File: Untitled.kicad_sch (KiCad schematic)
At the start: 1 part, among them U1 ICE40LP8K-CM121

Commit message: Move tinyfpga components to main schem
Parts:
- added C1, C10, C15, C6: 1uF, Capacitors_SMD:C_0402_NoSilk, symbol TinyFPGA-BX-rescue:C
- added C11, C16, C17: 100nF, Capacitors_SMD:C_0402_NoSilk, symbol TinyFPGA-BX-rescue:C
- added C12, C13, C7, C9: 10nF, Capacitors_SMD:C_0402_NoSilk, symbol TinyFPGA-BX-rescue:C_Small
- added C14, C2, C3, C4: 100nF, Capacitors_SMD:C_0402_NoSilk, symbol TinyFPGA-BX-rescue:C_Small
- added C5, C8: 10uF, Capacitors_SMD:C_0603, symbol TinyFPGA-BX-rescue:C
- added D1, D2: LED_Small, LEDs:LED_0603, symbol TinyFPGA-BX-rescue:LED_Small
- added J1: USB_OTG, Connectors:USB_Micro-B, symbol TinyFPGA-BX-rescue:USB_OTG
- added J2: Conn_02x03_Odd_Even, Pin_Headers:Pin_Header_Straight_2x03_Pitch2.54mm_SMD, symbol TinyFPGA-BX-rescue:Conn_02x03_Odd_Even
- added J3: Conn_02x08_Odd_Even, Pin_Headers:Pin_Header_Straight_2x08_Pitch2.54mm_SMD, symbol TinyFPGA-BX-rescue:Conn_02x08_Odd_Even
- added J4, J5: CONN_01X14, Pin_Headers:Pin_Header_Straight_1x14_Pitch2.54mm, symbol TinyFPGA-BX-rescue:Conn_01x14
- added L1: Bead, Inductors_SMD:L_0603, symbol TinyFPGA-BX-rescue:Ferrite_Bead_Small
- added R1: 100, Resistors_SMD:R_0402_NoSilk, symbol TinyFPGA-BX-rescue:R
- added R10, R7, R8: 10k, Resistors_SMD:R_0402_NoSilk, symbol TinyFPGA-BX-rescue:R
- added R2: 1.5k, Resistors_SMD:R_0402_NoSilk, symbol TinyFPGA-BX-rescue:R
- added R3, R4: 68, Resistors_SMD:R_0402_NoSilk, symbol TinyFPGA-BX-rescue:R
- added R5, R6: 270, Resistors_SMD:R_0402_NoSilk, symbol TinyFPGA-BX-rescue:R_Small
- added R9: R, Resistors_SMD:R_0402, symbol TinyFPGA-BX-rescue:R
- added SW1: SW_Push, tinyfpga:PTS_810_SMT_Switch, symbol TinyFPGA-BX-rescue:SW_Push
- added TP1, TP2, TP3: TEST, Measurement_Points:Measurement_Point_Round-SMD-Pad_Small, symbol TinyFPGA-BX-rescue:TEST
- added U2: MIC5504-3.3YM5-TR, tinyfpga:SC-70-C5, symbol TinyFPGA-BX-rescue:MIC5504-3.3YM5-TR
- added U3: MIC5365-1.2YC5-TR, tinyfpga:SC-70-C5, symbol TinyFPGA-BX-rescue:MIC5365-1.2YC5-TR
- added U4: iCE40-LP8K-CM81, tinyfpga:CM81, symbol TinyFPGA-BX-rescue:iCE40-LP8K-CM81
- added U5: DSC6001CI2A-016.0000T, tinyfpga:CDFN3225-4LD-PL-1, symbol TinyFPGA-BX-rescue:DSC6001CI2A-016.0000T
- added U6: AT25SF081-SSHD-B, Housings_SOIC:SOIC-8-1EP_3.9x4.9mm_Pitch1.27mm, symbol TinyFPGA-BX-rescue:AT25SF041-SSHD-B
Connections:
- new net: J1.2 (D-), R4.2
- new net: D1.1 (K), R5.1
- new net: C11.1, C8.1, U4.J6 (GNDPLL0)
- new net: C11.2, C8.2, R1.1, U4.J7 (VCCPLL0)
- new net: D2.1 (K), R6.1
- new net: J1.1 (VBUS), L1.2
- new net: J1.3 (D+), R2.1, R3.2
- new net +1V2: C15.1, C4.1, C7.1, C9.1, R1.2, TP1.1, U3.5 (VOUT), U4.D4 (VCC), U4.E3 (IOL_14A_GBIN6), U4.E9 (VCC), U4.F1 (IOL_22A), U4.F2 (VCC)
- new net +3V3: C10.1, C12.1, C13.1, C14.1, C16.1, C17.1, C2.1, C3.1, C6.1, D1.2 (A), J3.3 (Pin_3), J5.3 (Pin_3), R10.1, R7.1, R8.1, R9.1, U2.4 (NC), U2.5 (VOUT), U3.1 (VIN), U3.3 (EN), U4.A5 (VCCIO_0), U4.B5 (IOT_188), U4.B9 (IOR_120), U4.C6 (VCCIO_1), U4.C8 (VPP_2V5), U4.H3 (VCCIO_3), U4.H8 (VCC_SPI), U4.J5 (VCCIO_2), U5.1 (OE), U5.4 (VDD), U6.8 (VCC)
- new net +5V: C1.1, C5.1, J5.1 (Pin_1), L1.1, U2.1 (VIN), U2.3 (EN)
- new net 109: J3.9 (Pin_9), R8.2, U4.J8 (IOR_109), U6.7 (!HOLD)
- new net 10A: J4.8 (Pin_8), U4.D1 (IOL_10A)
- new net 10B: J4.10 (Pin_10), U4.E1 (IOL_10B)
- new net 110: J3.5 (Pin_5), U4.J9 (IOR_110)
- new net 111: J5.14 (Pin_14), U4.H9 (IOR_111)
- new net 112: J3.7 (Pin_7), U4.G9 (IOR_112)
- new net 115: U4.D6 (IOR_115)
- new net 116: J5.10 (Pin_10), U4.A9 (IOR_116)
- new net 119: J5.13 (Pin_13), U4.D9 (IOR_119)
- new net 13A: J4.9 (Pin_9), U4.E2 (IOL_13A)
- new net 140: J3.1 (Pin_1), U4.E8 (IOR_140_GBIN3)
- new net 141: J5.12 (Pin_12), U4.D8 (IOR_141_GBIN2)
- new net 148: J5.11 (Pin_11), U4.C9 (IOR_148)
- new net 170: J5.9 (Pin_9), U4.B8 (IOT_170)
- new net 174: J5.8 (Pin_8), U4.A8 (IOT_174)
- new net 177: J5.6 (Pin_6), U4.A7 (IOT_177)
- new net 180: J5.7 (Pin_7), U4.B7 (IOT_180)
- new net 183: J5.5 (Pin_5), U4.B6 (IOT_183)
- new net 185: J5.4 (Pin_4), U4.A6 (IOT_185)
- new net 212: U4.D5 (IOT_212)
- new net 221: J4.2 (Pin_2), U4.A2 (IOT_221)
- new net 224: J4.3 (Pin_3), U4.A1 (IOT_224)
- new net 24A: U4.G3 (IOL_24A)
- new net 24B: J3.2 (Pin_2), U4.G1 (IOL_24B)
- new net 26A: J4.11 (Pin_11), U4.G2 (IOL_26A)
- new net 26B: J4.14 (Pin_14), U4.H2 (IOL_26B)
- new net 2A: J4.5 (Pin_5), U4.C2 (IOL_2A)
- new net 3A: J4.4 (Pin_4), U4.B1 (IOL_3A)
- new net 3B: J4.6 (Pin_6), U4.C1 (IOL_3B)
- new net 54: J4.12 (Pin_12), U4.H1 (IOB_54)
- new net 55: J4.13 (Pin_13), U4.J1 (IOB_55)
- new net 56: J2.2 (Pin_2), U4.J2 (IOB_56)
- new net 57: J3.6 (Pin_6), U4.J3 (IOB_57)
- new net 70: J3.8 (Pin_8), U4.J4 (IOB_70)
- new net 7A: J4.7 (Pin_7), U4.D2 (IOL_7A)
- new net 81_GBIN5: U4.G4 (IOB_81_GBIN5)
- new net 82: J3.10 (Pin_10), R7.2, TP2.1, U4.H4 (IOB_82_GBIN4), U6.3 (!WP)
- new net CDONE: U4.E6 (CDONE)
- new net CLK: J2.1 (Pin_1), U4.B2 (IOL_2B), U5.3 (OUT)
- new net CRESET_B: R9.2, SW1.2, TP3.1, U4.H6 (CRESET_B)
- new net GND: C1.2, C10.2, C12.2, C13.2, C14.2, C15.2, C16.2, C17.2, C2.2, C3.2, C4.2, C5.2, C6.2, C7.2, C9.2, J1.5 (GND), J1.6 (Shield), J3.15 (Pin_15), J3.16 (Pin_16), J3.4 (Pin_4), J4.1 (Pin_1), J5.2 (Pin_2), R5.2, R6.2, SW1.1, U2.2 (GND), U3.2 (GND), U4.E4 (IOL_14B), U4.E5 (IOT_214), U4.F4 (GND), U4.F5 (GND), U4.F6 (GND), U4.F9 (GND), U5.2 (GND), U6.4 (GND)
- new net LED: D2.2 (A), J2.3 (Pin_3), U4.B3 (IOT_218)
- new net SCK: J3.11 (Pin_11), U4.G7 (IOB_107_SCK), U4.G8 (IOR_114), U6.6 (SCK)
- new net SDI: J3.12 (Pin_12), U4.H7 (IOB_106_SDI), U6.2 (SO)
- new net SDO: J3.13 (Pin_13), U4.G6 (IOB_105_SDO), U4.H5 (IOB_104_CBSEL1), U6.5 (SI)
- new net SS: J3.14 (Pin_14), R10.2, U4.F7 (IOB_108_SS), U4.F8 (IOR_113), U6.1 (!CS)
- new net USB_N: J2.6 (Pin_6), R4.1, U4.A4 (IOT_208)
- new net USB_P: J2.5 (Pin_5), R3.1, U4.B4 (IOT_211)
- new net USB_PU: J2.4 (Pin_4), R2.2, U4.A3 (IOT_217)
- new net VPP_FAST: U4.C7 (VPP_FAST)
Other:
- note added: "16MHz Clock"
- note added: "FPGA PLL decoupling capacitors"
- note added: "FPGA connections"
- note added: "FPGA core and IO power connections and decoupling capacitors"
- note added: "FPGA reset button and testpoint"
- note added: "SPI flash memory for FPGA configuration"
- note added: "TinyFPGA Bx Pin Headers"
- note added: "USB connection and power filtering"
- note added: "Voltage Regulation"
- moved on the sheet: U1A, U1B, U1C, U1D, U1E, U1F

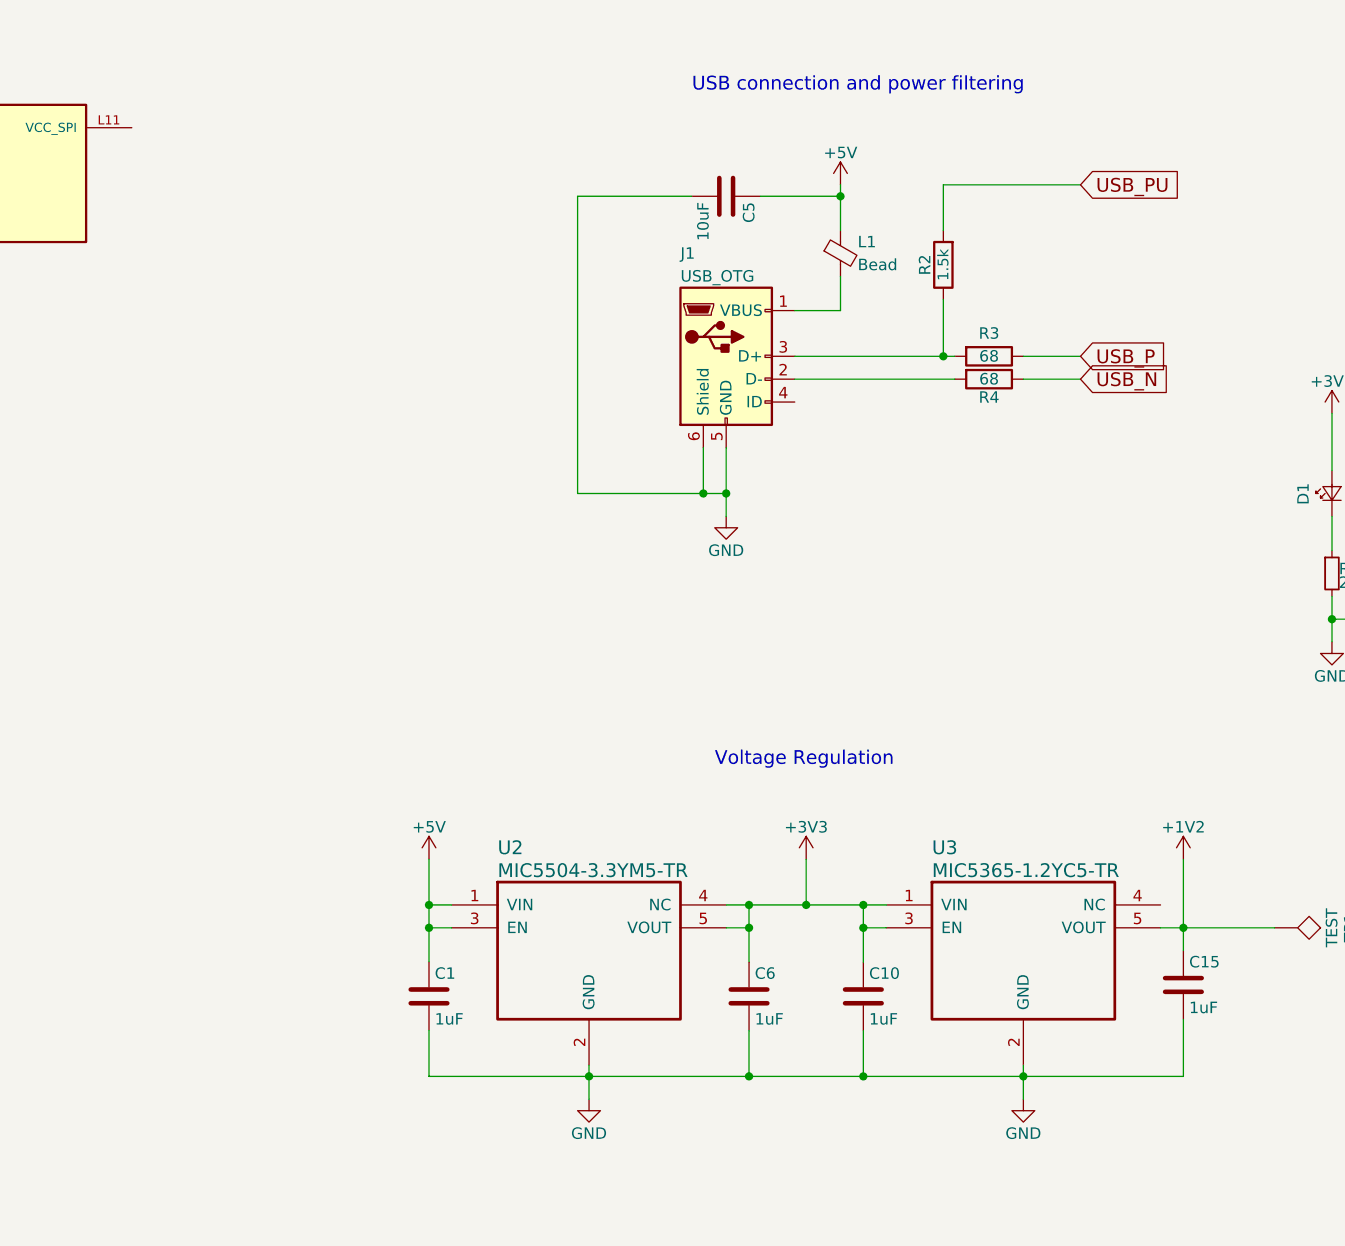
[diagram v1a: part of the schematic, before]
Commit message: Switch usb, LDOs
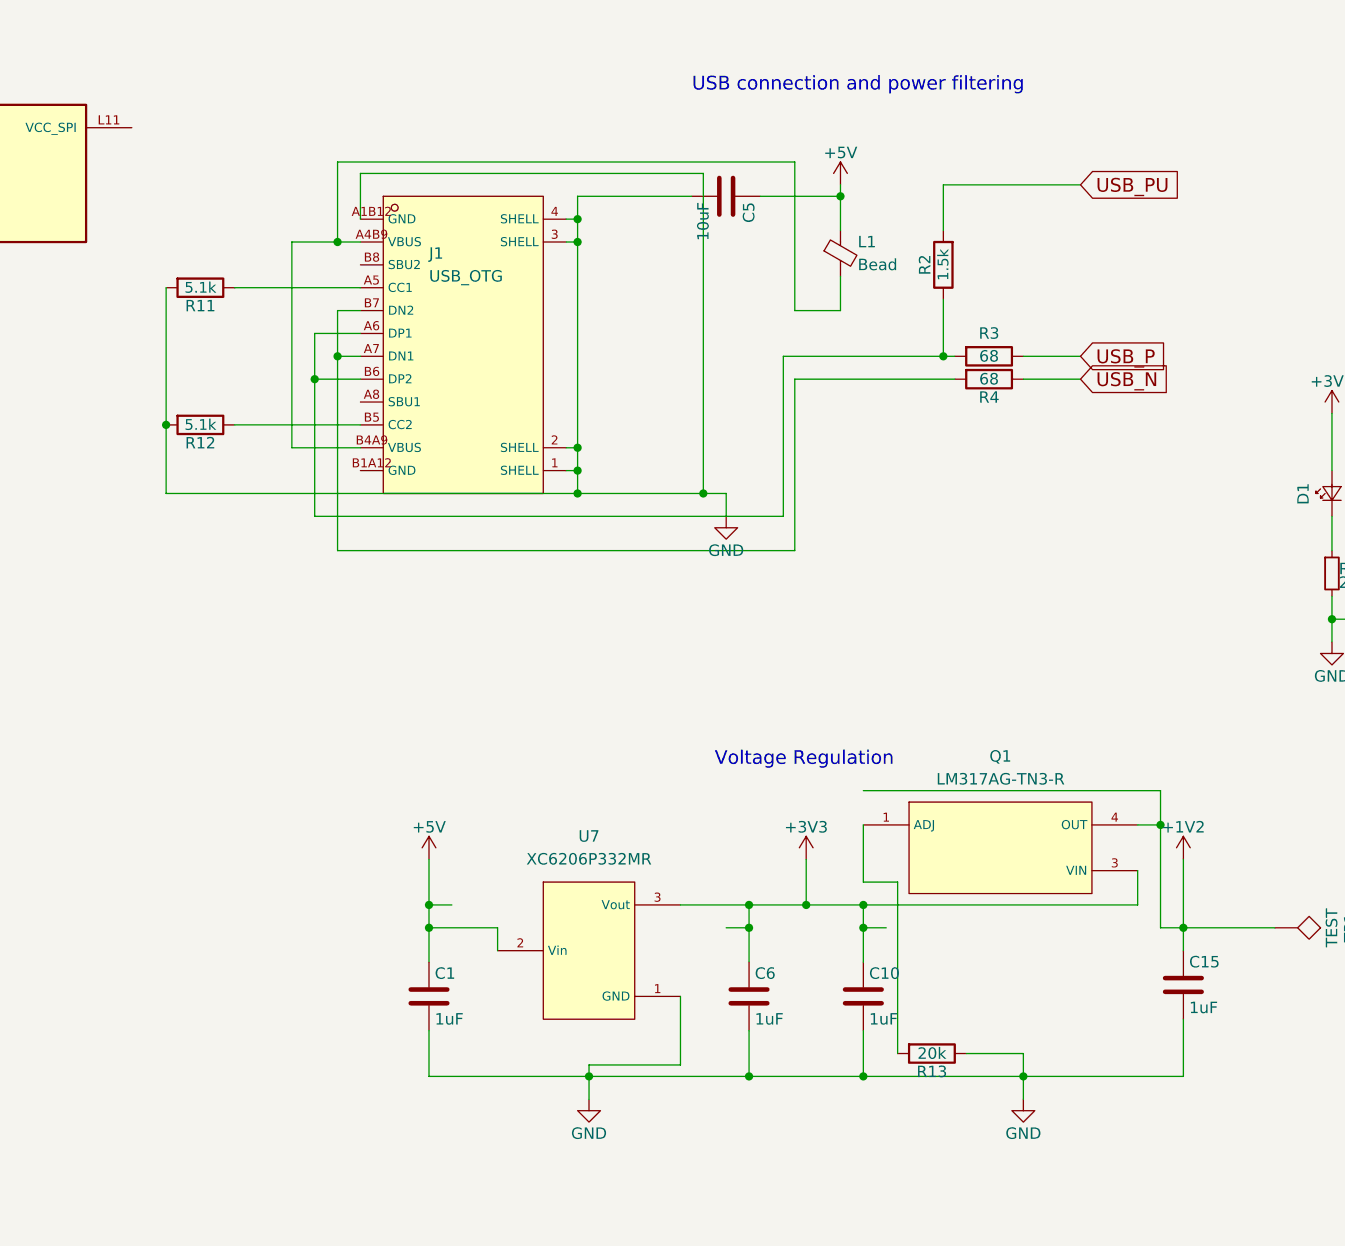
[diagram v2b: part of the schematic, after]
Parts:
- removed U2: MIC5504-3.3YM5-TR, tinyfpga:SC-70-C5, symbol TinyFPGA-BX-rescue:MIC5504-3.3YM5-TR
- removed U3: MIC5365-1.2YC5-TR, tinyfpga:SC-70-C5, symbol TinyFPGA-BX-rescue:MIC5365-1.2YC5-TR
- added Q1: LM317AG-TN3-R, footprint:TO-252-2_L6.5-W6.1-P4.58-LS10.0-TL, symbol LM317AG-TN3-R:LM317AG-TN3-R
- added R11, R12: 5.1k, Resistors_SMD:R_0402_NoSilk, symbol TinyFPGA-BX-rescue:R
- added R13: 20k, Resistors_SMD:R_0402_NoSilk, symbol TinyFPGA-BX-rescue:R
- added U7: XC6206P332MR, footprint:SOT-23-3_L2.9-W1.6-P1.90-LS2.8-BR, symbol XC6206P332MR:XC6206P332MR
- J1: footprint Connectors:USB_Micro-B -> footprint:USB-C-SMD_G-SWITCH_GT-USB-7010ASV; symbol TinyFPGA-BX-rescue:USB_OTG -> GT-USB-7010ASV:GT-USB-7010ASV; LCSC (none) -> C2988369
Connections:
- net +1V2: now also Q1.4 (OUT)
- net +3V3: now also Q1.3 (VIN), U7.3 (Vout)
- net +5V: now also U7.2 (Vin)
- net GND: now also J1.1 (SHELL), J1.2 (SHELL), J1.3 (SHELL), J1.4 (SHELL), J1.A1B12 (GND), R11.2, R12.2, R13.1, U7.1 (GND); no longer J1.5 (GND), J1.6 (Shield)
- net at R4.2: now also J1.A7 (DN1), J1.B7 (DN2); no longer J1.2 (D-)
- net at L1.2: now also J1.A4B9 (VBUS), J1.B4A9 (VBUS); no longer J1.1 (VBUS)
- net at R2.1, R3.2: now also J1.A6 (DP1), J1.B6 (DP2); no longer J1.3 (D+)
- new net: J1.A5 (CC1), R11.1
- new net: Q1.1 (ADJ), R13.2
- new net: J1.B5 (CC2), R12.1

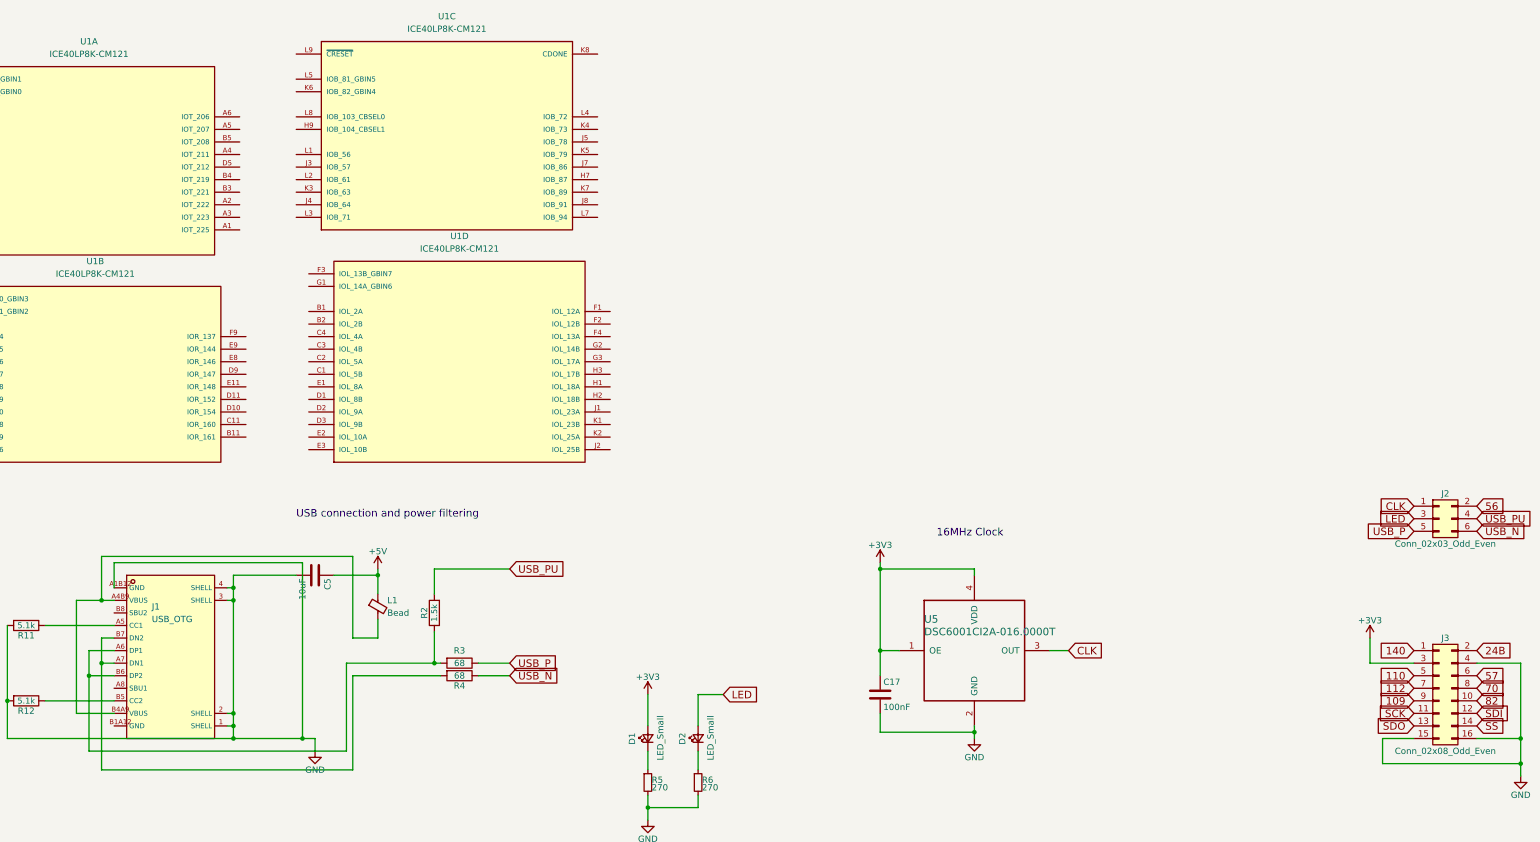
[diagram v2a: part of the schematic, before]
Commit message: Hook up some data pins to usb-c
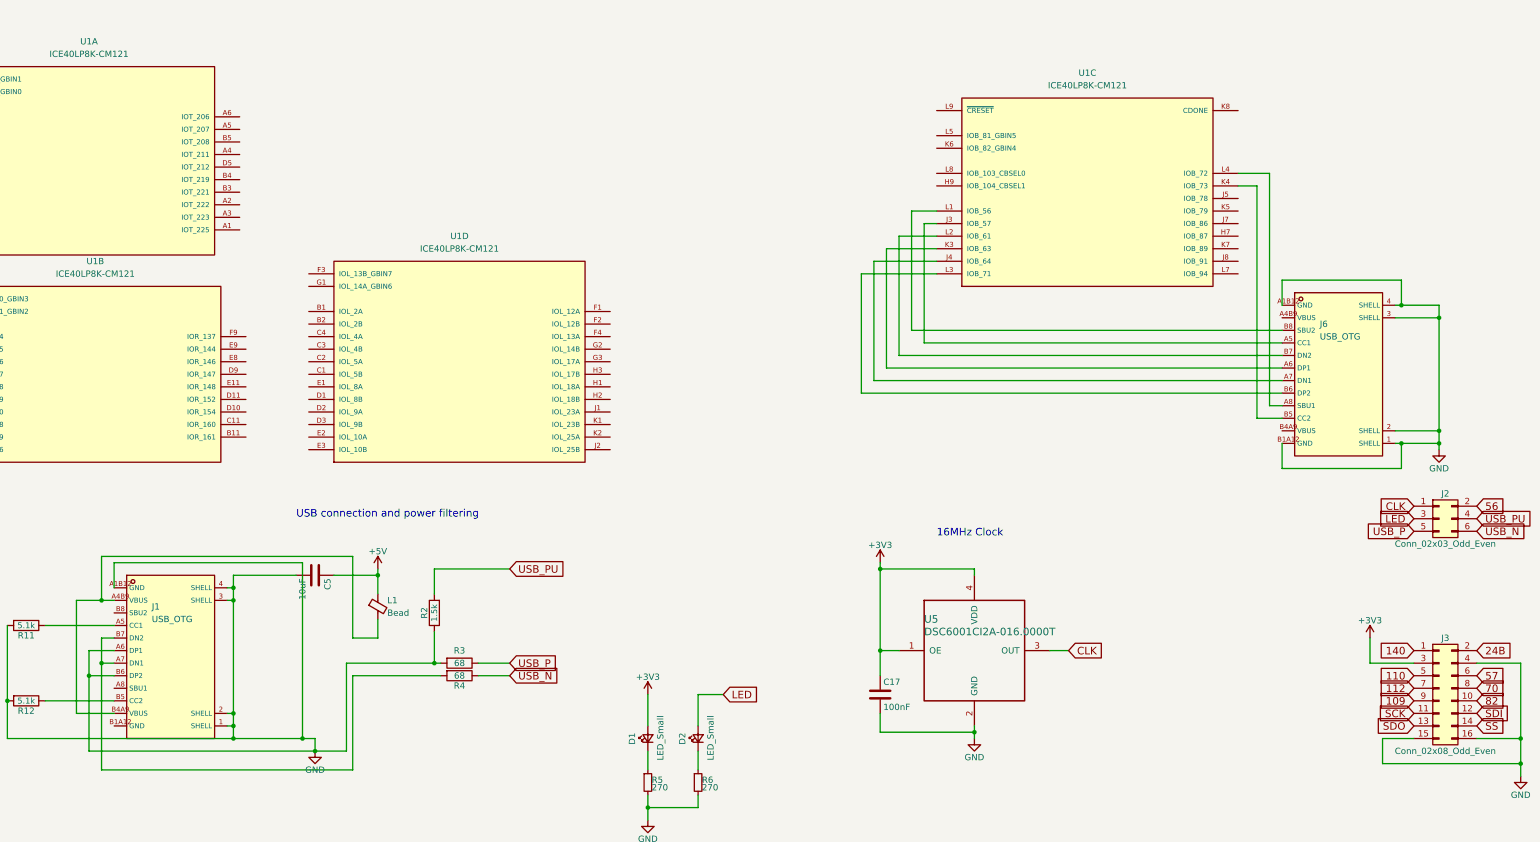
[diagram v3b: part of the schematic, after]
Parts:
- added J6: USB_OTG, footprint:USB-C-SMD_G-SWITCH_GT-USB-7010ASV, symbol GT-USB-7010ASV:GT-USB-7010ASV
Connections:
- net GND: now also J1.A6 (DP1), J1.B6 (DP2), R2.1, R3.2, J6.1 (SHELL), J6.2 (SHELL), J6.3 (SHELL), J6.4 (SHELL), J6.A1B12 (GND), J6.B1A12 (GND)
- net at U1.J3 (IOB_57): now also J6.A5 (CC1)
- net at U1.J4 (IOB_64): now also J6.A7 (DN1)
- net at U1.K3 (IOB_63): now also J6.A6 (DP1)
- net at U1.K4 (IOB_73): now also J6.B5 (CC2)
- net at U1.L1 (IOB_56): now also J6.B8 (SBU2)
- net at U1.L2 (IOB_61): now also J6.B7 (DN2)
- net at U1.L3 (IOB_71): now also J6.B6 (DP2)
- net at U1.L4 (IOB_72): now also J6.A8 (SBU1)
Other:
- moved on the sheet: U1C
